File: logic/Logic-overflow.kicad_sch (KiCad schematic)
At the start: 19 parts, among them J4 Conn_02x05_Odd_Even, U14 74HC14

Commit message: Complete schematic and begin logic board layout.
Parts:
- added C15: C, Capacitor_THT:C_Disc_D3.4mm_W2.1mm_P2.50mm, symbol Device:C
- C1: footprint Capacitor_THT:C_Disc_D3.4mm_W2.1mm_P2.50mm -> Capacitor_THT:CP_Radial_D8.0mm_P2.50mm
- renumbered C20 to C10, C22 to C11, C24 to C12, C26 to C13, C28 to C14, C18 to C4, C19 to C5, C21 to C6, C23 to C7, C25 to C8, C27 to C9
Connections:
- net HV_REG is gone; now on net GND: S1.4 (PGND)
- net GND: now also C15.2; no longer S1.2 (LGND), U14.3
- net POR: now reaches U14.4
- net LV_REG renamed V5.0
- net V5.0: now also C10.1, C11.1, C12.1, C13.1, C14.1, C5.1, C6.1, C7.1, C8.1, C9.1, R4.1, S1.2 (LV_IN), U14.14 (VCC), C15.1
- removed net VCC: C10.1, C11.1, C12.1, C13.1, C14.1, C5.1, C6.1, C7.1, C8.1, C9.1, R4.1, S1.1 (LV_IN), U14.14 (VCC)
- net ~{POR}: no longer names the net of U14.12
- net ~{POR}: now also U14.3
- new net V170: S1.1 (HV_OUT)
- no-connect marks 4 -> 3
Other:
- moved on the sheet: S1, U14B, U14G

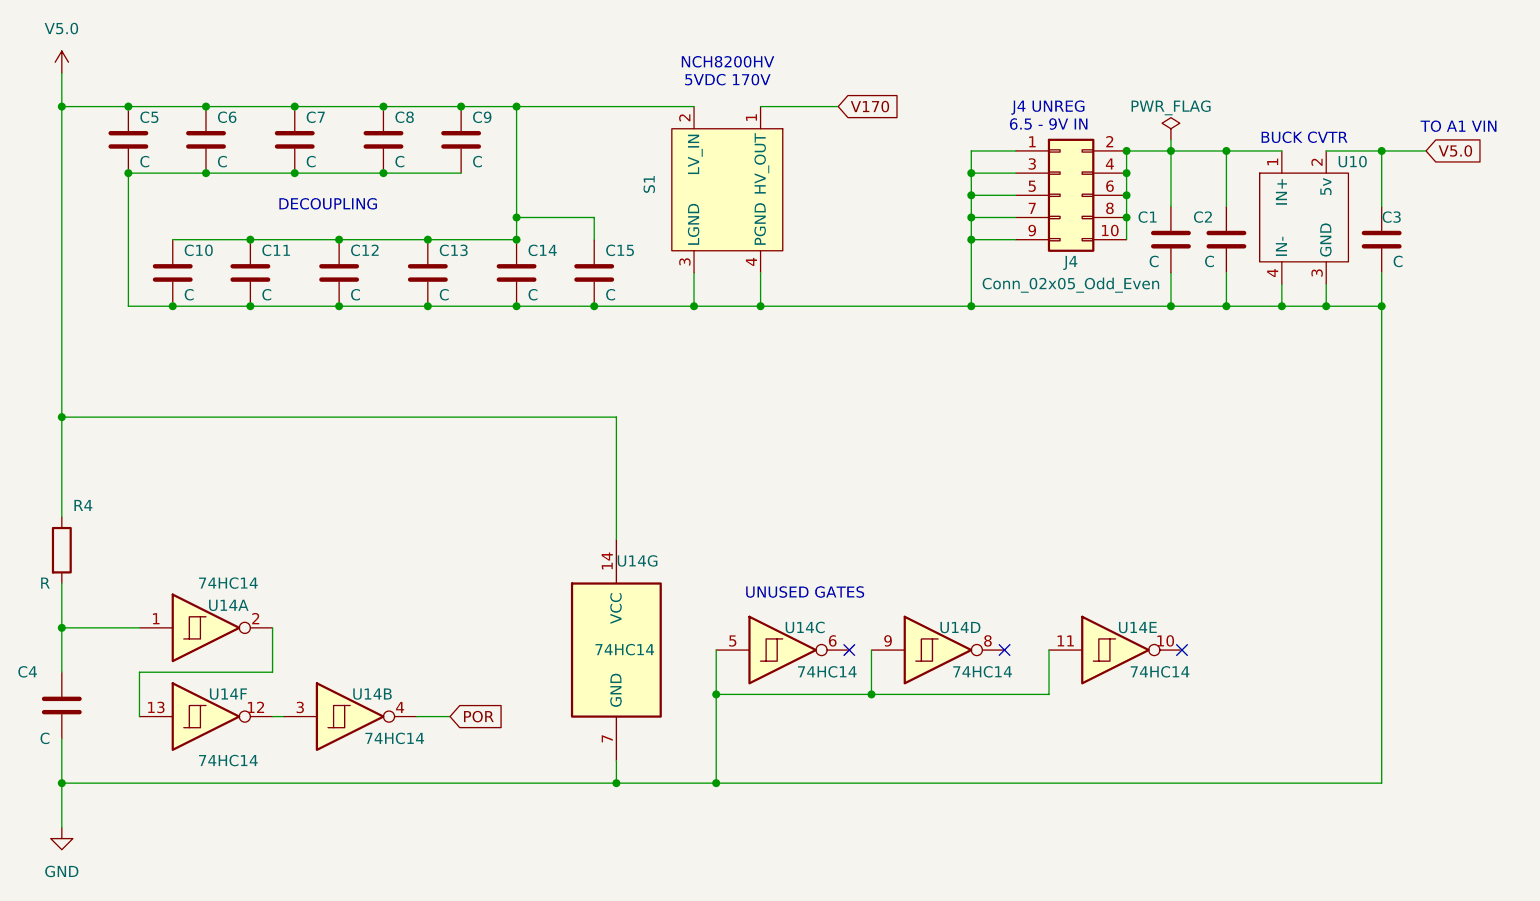
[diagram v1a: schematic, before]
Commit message: Ongoing development. Add shunt resistors to display board.
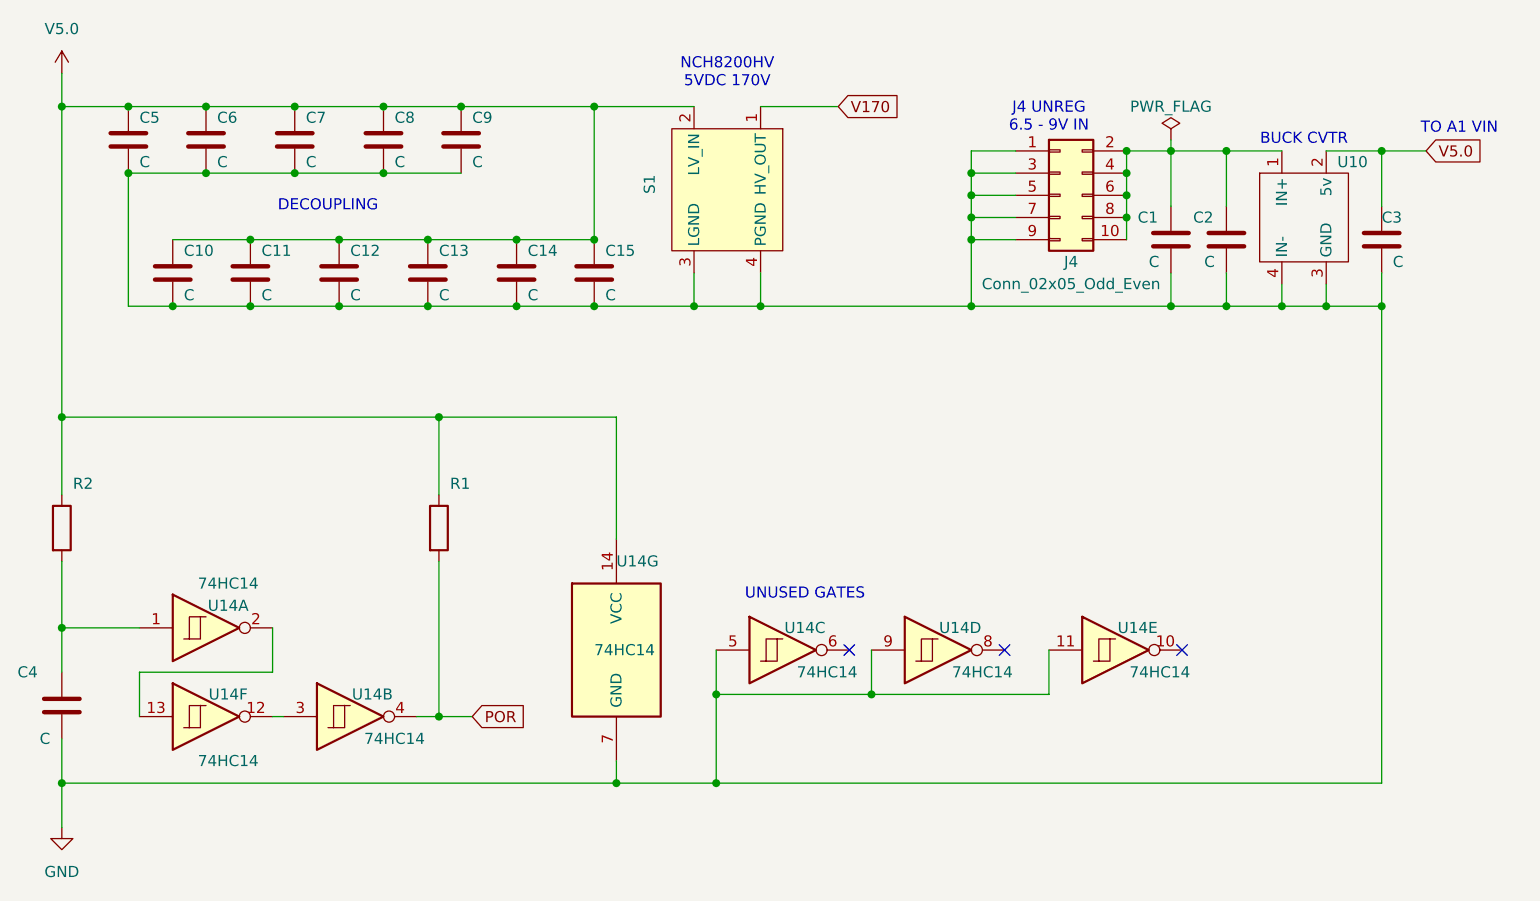
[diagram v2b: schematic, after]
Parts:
- added R1: R, Resistor_THT:R_Axial_DIN0207_L6.3mm_D2.5mm_P10.16mm_Horizontal, symbol Device:R
- renumbered R4 to R2
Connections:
- net POR: now also R1.2
- net V5.0: now also R1.1
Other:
- moved on the sheet: R2
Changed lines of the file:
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@@
 	)
 	(junction
+		(at 105.41 128.27)
+		(diameter 0)
+		(color 0 0 0 0)
+	)
+	(junction
 		(at 213.36 81.28)
 		(diameter 0)
@@
 	)
 	(junction
+		(at 123.19 58.42)
+		(diameter 0)
+		(color 0 0 0 0)
+	)
+	(junction
 		(at 114.3 81.28)
 		(diameter 0)
@@
 	)
 	(junction
-		(at 93.98 81.28)
-		(diameter 0)
-		(color 0 0 0 0)
-	)
-	(junction
-		(at 114.3 71.12)
+		(at 105.41 93.98)
 		(diameter 0)
 		(color 0 0 0 0)
 	)
 	(junction
-		(at 114.3 58.42)
+		(at 93.98 81.28)
 		(diameter 0)
 		(color 0 0 0 0)
@@
 		(color 0 0 0 0)
 	)
+	(junction
+		(at 123.19 73.66)
+		(diameter 0)
+		(color 0 0 0 0)
+	)
 	(no_connect
 		(at 170.18 120.65)
@@
 	(wire
 		(pts
-			(xy 114.3 58.42) (xy 134.62 58.42)
+			(xy 137.16 120.65) (xy 137.16 125.73)
 		)
 		(stroke
@@
 	(wire
 		(pts
-			(xy 137.16 120.65) (xy 137.16 125.73)
+			(xy 166.37 73.66) (xy 166.37 81.28)
 		)
 		(stroke
@@
 	(wire
 		(pts
-			(xy 166.37 73.66) (xy 166.37 81.28)
+			(xy 207.01 81.28) (xy 213.36 81.28)
 		)
 		(stroke
@@
 	(wire
 		(pts
-			(xy 207.01 81.28) (xy 213.36 81.28)
+			(xy 102.87 128.27) (xy 105.41 128.27)
 		)
 		(stroke
@@
 	(wire
 		(pts
-			(xy 102.87 128.27) (xy 106.68 128.27)
+			(xy 105.41 93.98) (xy 125.73 93.98)
 		)
 		(stroke
@@
 	(wire
 		(pts
+			(xy 105.41 93.98) (xy 105.41 102.87)
+		)
+		(stroke
+			(width 0)
+			(type default)
+		)
+	)
+	(wire
+		(pts
 			(xy 137.16 125.73) (xy 154.94 125.73)
 		)
@@
 	(wire
 		(pts
+			(xy 105.41 128.27) (xy 109.22 128.27)
+		)
+		(stroke
+			(width 0)
+			(type default)
+		)
+	)
+	(wire
+		(pts
 			(xy 195.58 81.28) (xy 201.93 81.28)
 		)
@@
 	(wire
 		(pts
-			(xy 62.23 113.03) (xy 62.23 118.11)
+			(xy 62.23 110.49) (xy 62.23 118.11)
 		)
 		(stroke
@@
 	(wire
 		(pts
-			(xy 114.3 58.42) (xy 114.3 71.12)
-		)
-		(stroke
-			(width 0)
-			(type default)
-		)
-	)
-	(wire
-		(pts
 			(xy 62.23 118.11) (xy 62.23 123.19)
 		)
@@
 	(wire
 		(pts
-			(xy 123.19 71.12) (xy 114.3 71.12)
+			(xy 123.19 73.66) (xy 114.3 73.66)
 		)
 		(stroke
@@
 	(wire
 		(pts
-			(xy 107.95 58.42) (xy 114.3 58.42)
+			(xy 107.95 58.42) (xy 123.19 58.42)
 		)
 		(stroke
@@
 	(wire
 		(pts
-			(xy 123.19 71.12) (xy 123.19 73.66)
+			(xy 105.41 110.49) (xy 105.41 128.27)
 		)
 		(stroke
@@
 	(wire
 		(pts
-			(xy 213.36 63.5) (xy 218.44 63.5)
+			(xy 123.19 58.42) (xy 134.62 58.42)
 		)
 		(stroke
@@
 	(wire
 		(pts
-			(xy 142.24 58.42) (xy 151.13 58.42)
+			(xy 213.36 63.5) (xy 218.44 63.5)
 		)
 		(stroke
@@
 	(wire
 		(pts
-			(xy 166.37 68.58) (xy 166.37 71.12)
+			(xy 142.24 58.42) (xy 151.13 58.42)
 		)
 		(stroke
@@
 	(wire
 		(pts
-			(xy 114.3 71.12) (xy 114.3 73.66)
+			(xy 166.37 68.58) (xy 166.37 71.12)
 		)
 		(stroke
@@
 	(wire
 		(pts
-			(xy 62.23 93.98) (xy 62.23 105.41)
+			(xy 62.23 93.98) (xy 62.23 102.87)
 		)
 		(stroke
@@
 	(wire
 		(pts
+			(xy 123.19 58.42) (xy 123.19 73.66)
+		)
+		(stroke
+			(width 0)
+			(type default)
+		)
+	)
+	(wire
+		(pts
 			(xy 189.23 81.28) (xy 195.58 81.28)
 		)
@@
 	(wire
 		(pts
-			(xy 62.23 93.98) (xy 125.73 93.98)
+			(xy 62.23 93.98) (xy 105.41 93.98)
 		)
 		(stroke
@@
 	(global_label "POR"
 		(shape input)
-		(at 106.68 128.27 0)
+		(at 109.22 128.27 0)
 		(fields_autoplaced yes)
 		(effects
@@
 		)
 		(property "Intersheetrefs" "${INTERSHEET_REFS}"
-			(at 113.5357 128.27 0)
+			(at 116.0757 128.27 0)
 			(effects
 				(font
@@
 	(symbol
 		(lib_id "Device:R")
-		(at 62.23 109.22 0)
+		(at 62.23 106.68 0)
 		(unit 1)
 		(exclude_from_sim no)
@@
 		(on_board yes)
 		(dnp no)
-		(property "Reference" "R4"
-			(at 63.5 104.14 0)
+		(property "Reference" "R2"
+			(at 63.5 101.6 0)
 			(effects
 				(font
@@
 		)
 		(property "Value" "R"
-			(at 59.69 113.03 0)
+			(at 59.69 110.49 0)
 			(effects
 				(font
@@
 				)
 				(justify left)
+				(hide yes)
 			)
 		)
 		(property "Footprint" "Resistor_THT:R_Axial_DIN0207_L6.3mm_D2.5mm_P10.16mm_Horizontal"
-			(at 60.452 109.22 90)
+			(at 60.452 106.68 90)
 			(effects
 				(font
@@
 		)
 		(property "Datasheet" "~"
-			(at 62.23 109.22 0)
+			(at 62.23 106.68 0)
 			(effects
 				(font
@@
 		)
 		(property "Description" "Resistor"
-			(at 62.23 109.22 0)
+			(at 62.23 106.68 0)
 			(effects
 				(font
@@
 			(project "logic"
 				(path "/4078bfcf-e5c1-4f0e-b66f-b232c5a6fa8f/abcbf27b-3dee-4ee8-964d-79d185d384bd"
-					(reference "R4")
+					(reference "R2")
 					(unit 1)
 				)
@@
 					(unit 1)
 				)
+			)
+		)
+	)
+	(symbol
+		(lib_id "Device:R")
+		(at 105.41 106.68 0)
+		(unit 1)
+		(exclude_from_sim no)
+		(in_bom yes)
+		(on_board yes)
+		(dnp no)
+		(property "Reference" "R1"
+			(at 106.68 101.6 0)
+			(effects
+				(font
+					(size 1.27 1.27)
+				)
+				(justify left)
+			)
+		)
+		(property "Value" "R"
+			(at 102.87 110.49 0)
+			(effects
+				(font
+					(size 1.27 1.27)
+				)
+				(justify left)
+				(hide yes)
+			)
+		)
+		(property "Footprint" "Resistor_THT:R_Axial_DIN0207_L6.3mm_D2.5mm_P10.16mm_Horizontal"
+			(at 103.632 106.68 90)
+			(effects
+				(font
+					(size 1.27 1.27)
+				)
+				(hide yes)
+			)
+		)
+		(property "Datasheet" "~"
+			(at 105.41 106.68 0)
+			(effects
+				(font
+					(size 1.27 1.27)
+				)
+				(hide yes)
+			)
+		)
+		(property "Description" "Resistor"
+			(at 105.41 106.68 0)
+			(effects
+				(font
+					(size 1.27 1.27)
+				)
+				(hide yes)
+			)
+		)
+		(pin "2"
+		)
+		(pin "1"
+		)
+		(instances
+			(project "logic"
+				(path "/4078bfcf-e5c1-4f0e-b66f-b232c5a6fa8f/abcbf27b-3dee-4ee8-964d-79d185d384bd"
+					(reference "R1")
+					(unit 1)
+				)

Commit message: Ongoing development
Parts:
- U14: footprint Package_DIP:DIP-14_W7.62mm_Socket -> Package_DIP:DIP-14_W7.62mm_Socket_LongPads
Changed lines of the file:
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@@
 			)
 		)
-		(property "Footprint" "Package_DIP:DIP-14_W7.62mm_Socket"
+		(property "Footprint" "Package_DIP:DIP-14_W7.62mm_Socket_LongPads"
 			(at 78.74 128.27 0)
 			(effects
@@
 			)
 		)
-		(property "Footprint" "Package_DIP:DIP-14_W7.62mm_Socket"
+		(property "Footprint" "Package_DIP:DIP-14_W7.62mm_Socket_LongPads"
 			(at 182.88 120.65 0)
 			(effects
@@
 			)
 		)
-		(property "Footprint" "Package_DIP:DIP-14_W7.62mm_Socket"
+		(property "Footprint" "Package_DIP:DIP-14_W7.62mm_Socket_LongPads"
 			(at 95.25 128.27 0)
 			(effects
@@
 			)
 		)
-		(property "Footprint" "Package_DIP:DIP-14_W7.62mm_Socket"
+		(property "Footprint" "Package_DIP:DIP-14_W7.62mm_Socket_LongPads"
 			(at 162.56 120.65 0)
 			(effects
@@
 			)
 		)
-		(property "Footprint" "Package_DIP:DIP-14_W7.62mm_Socket"
+		(property "Footprint" "Package_DIP:DIP-14_W7.62mm_Socket_LongPads"
 			(at 78.74 118.11 0)
 			(effects
@@
 			)
 		)
-		(property "Footprint" "Package_DIP:DIP-14_W7.62mm_Socket"
+		(property "Footprint" "Package_DIP:DIP-14_W7.62mm_Socket_LongPads"
 			(at 144.78 120.65 0)
 			(effects
@@
 			)
 		)
-		(property "Footprint" "Package_DIP:DIP-14_W7.62mm_Socket"
+		(property "Footprint" "Package_DIP:DIP-14_W7.62mm_Socket_LongPads"
 			(at 125.73 120.65 0)
 			(effects
